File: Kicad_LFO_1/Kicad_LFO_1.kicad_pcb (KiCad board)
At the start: 2 copper layers, 100 x 100 mm, 13 parts, among them J101 LFO555, J102 555 Reset, J103 LFO555Charge, SW101 LFO Low, U101 LM555

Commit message: Sine and tri integrator added
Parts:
- added P101: HEADER_2x5_Doepfer, Connector_IDC:IDC-Header_2x05_P2.54mm_Vertical, F.Cu at (62.0, 144.5)
- added U102: TL072, AJ-Dropbox-Kicad:AJ_SO-8_5.3x6.2mm_P1.27mm, B.Cu at (58.5, 114.5)
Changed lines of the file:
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@@
     (tracks 0)
     (zones 0)
-    (modules 13)
-    (nets 12)
+    (modules 15)
+    (nets 14)
   )
   (page A4)
@@
     (solder_mask_min_width 0.25)
     (aux_axis_origin 0 0)
-    (visible_elements FFFFFF7F)
+    (visible_elements 7FFFFFFF)
     (pcbplotparams
       (layerselection 0x010fc_ffffffff)
@@
   (net 10 "Net-(J102-PadT)")
   (net 11 "Net-(RV101-Pad2)")
+  (net 12 -12V)
+  (net 13 "Net-(P101-Pad10)")
   (net_class Default "This is the default net class."
     (clearance 0.2)
@@
     (uvia_drill 0.1)
     (add_net +12V)
+    (add_net -12V)
     (add_net GND)
     (add_net "Net-(C101-Pad1)")
@@
     (add_net "Net-(J101-PadT)")
     (add_net "Net-(J102-PadT)")
+    (add_net "Net-(P101-Pad10)")
     (add_net "Net-(R101-Pad1)")
     (add_net "Net-(R102-Pad1)")
@@
     (model ${KISYS3DMOD}/Package_SO.3dshapes/SO-8_5.3x6.2mm_P1.27mm.wrl
       (at (xyz 0 0 0))
+      (scale (xyz 1 1 1))
+      (rotate (xyz 0 0 0))
+    )
+    (model C:/Users/anders/Documents/KiCad/Lib/aj_packages3d/kicad-packages3D/Package_SO.3dshapes/SO-8_5.3x6.2mm_P1.27mm.step
+      (at (xyz 0 0 0))
+      (scale (xyz 1 1 1))
+      (rotate (xyz 0 0 0))
+    )
+  )
+  (module Connector_IDC:IDC-Header_2x05_P2.54mm_Vertical (layer F.Cu)
+    (at 62 144.5 180)
+    (descr "Through hole straight IDC box header, 2x05, 2.54mm pitch, double rows")
+    (tags "Through hole IDC box header THT 2x05 2.54mm double row")
+    (fp_text reference P101 (at 1.27 -6.604 180) (layer F.SilkS)
+      (effects (font (size 1 1) (thickness 0.15)))
+    )
+    (fp_text value HEADER_2x5_Doepfer (at 1.27 16.764 180) (layer F.Fab)
+      (effects (font (size 1 1) (thickness 0.15)))
+    )
+    (fp_text user %R (at 1.27 5.08 180) (layer F.Fab)
+      (effects (font (size 1 1) (thickness 0.15)))
+    )
+    (fp_line (start 5.695 -5.1) (end 5.695 15.26) (layer F.Fab) (width 0.1))
+    (fp_line (start 5.145 -4.56) (end 5.145 14.7) (layer F.Fab) (width 0.1))
+    (fp_line (start -3.155 -5.1) (end -3.155 15.26) (layer F.Fab) (width 0.1))
+    (fp_line (start -2.605 -4.56) (end -2.605 2.83) (layer F.Fab) (width 0.1))
+    (fp_line (start -2.605 7.33) (end -2.605 14.7) (layer F.Fab) (width 0.1))
+    (fp_line (start -2.605 2.83) (end -3.155 2.83) (layer F.Fab) (width 0.1))
+    (fp_line (start -2.605 7.33) (end -3.155 7.33) (layer F.Fab) (width 0.1))
+    (fp_line (start 5.695 -5.1) (end -3.155 -5.1) (layer F.Fab) (width 0.1))
+    (fp_line (start 5.145 -4.56) (end -2.605 -4.56) (layer F.Fab) (width 0.1))
+    (fp_line (start 5.695 15.26) (end -3.155 15.26) (layer F.Fab) (width 0.1))
+    (fp_line (start 5.145 14.7) (end -2.605 14.7) (layer F.Fab) (width 0.1))
+    (fp_line (start 5.695 -5.1) (end 5.145 -4.56) (layer F.Fab) (width 0.1))
+    (fp_line (start 5.695 15.26) (end 5.145 14.7) (layer F.Fab) (width 0.1))
+    (fp_line (start -3.155 -5.1) (end -2.605 -4.56) (layer F.Fab) (width 0.1))
+    (fp_line (start -3.155 15.26) (end -2.605 14.7) (layer F.Fab) (width 0.1))
+    (fp_line (start 5.95 -5.35) (end 5.95 15.51) (layer F.CrtYd) (width 0.05))
+    (fp_line (start 5.95 15.51) (end -3.41 15.51) (layer F.CrtYd) (width 0.05))
+    (fp_line (start -3.41 15.51) (end -3.41 -5.35) (layer F.CrtYd) (width 0.05))
+    (fp_line (start -3.41 -5.35) (end 5.95 -5.35) (layer F.CrtYd) (width 0.05))
+    (fp_line (start 5.945 -5.35) (end 5.945 15.51) (layer F.SilkS) (width 0.12))
+    (fp_line (start 5.945 15.51) (end -3.405 15.51) (layer F.SilkS) (width 0.12))
+    (fp_line (start -3.405 15.51) (end -3.405 -5.35) (layer F.SilkS) (width 0.12))
+    (fp_line (start -3.405 -5.35) (end 5.945 -5.35) (layer F.SilkS) (width 0.12))
+    (fp_line (start -3.655 -5.6) (end -3.655 -3.06) (layer F.SilkS) (width 0.12))
+    (fp_line (start -3.655 -5.6) (end -1.115 -5.6) (layer F.SilkS) (width 0.12))
+    (pad 1 thru_hole rect (at 0 0 180) (size 1.7272 1.7272) (drill 1.016) (layers *.Cu *.Mask)
+      (net 12 -12V))
+    (pad 2 thru_hole oval (at 2.54 0 180) (size 1.7272 1.7272) (drill 1.016) (layers *.Cu *.Mask)
+      (net 12 -12V))
+    (pad 3 thru_hole oval (at 0 2.54 180) (size 1.7272 1.7272) (drill 1.016) (layers *.Cu *.Mask)
+      (net 1 GND))
+    (pad 4 thru_hole oval (at 2.54 2.54 180) (size 1.7272 1.7272) (drill 1.016) (layers *.Cu *.Mask)
+      (net 1 GND))
+    (pad 5 thru_hole oval (at 0 5.08 180) (size 1.7272 1.7272) (drill 1.016) (layers *.Cu *.Mask)
+      (net 1 GND))
+    (pad 6 thru_hole oval (at 2.54 5.08 180) (size 1.7272 1.7272) (drill 1.016) (layers *.Cu *.Mask)
+      (net 1 GND))
+    (pad 7 thru_hole oval (at 0 7.62 180) (size 1.7272 1.7272) (drill 1.016) (layers *.Cu *.Mask)
+      (net 1 GND))
+    (pad 8 thru_hole oval (at 2.54 7.62 180) (size 1.7272 1.7272) (drill 1.016) (layers *.Cu *.Mask)
+      (net 1 GND))
+    (pad 9 thru_hole oval (at 0 10.16 180) (size 1.7272 1.7272) (drill 1.016) (layers *.Cu *.Mask)
+      (net 13 "Net-(P101-Pad10)"))
+    (pad 10 thru_hole oval (at 2.54 10.16 180) (size 1.7272 1.7272) (drill 1.016) (layers *.Cu *.Mask)
+      (net 13 "Net-(P101-Pad10)"))
+    (model ${KISYS3DMOD}/Connector_IDC.3dshapes/IDC-Header_2x05_P2.54mm_Vertical.wrl
+      (at (xyz 0 0 0))
+      (scale (xyz 1 1 1))
+      (rotate (xyz 0 0 0))
+    )
+  )
+  (module AJ-Dropbox-Kicad:AJ_SO-8_5.3x6.2mm_P1.27mm (layer B.Cu)
+    (at 58.5 114.5)
+    (descr "8-Lead Plastic Small Outline, 5.3x6.2mm Body (http://www.ti.com.cn/cn/lit/ds/symlink/tl7705a.pdf)")
+    (tags "SOIC 1.27")
+    (attr smd)
+    (fp_text reference U102 (at 0 4.13) (layer B.SilkS)
+      (effects (font (size 1 1) (thickness 0.15)) (justify mirror))
+    )
+    (fp_text value TL072 (at 0 -4.13) (layer B.Fab)
+      (effects (font (size 1 1) (thickness 0.15)) (justify mirror))
+    )
+    (fp_text user %R (at 0 0) (layer B.Fab)
+      (effects (font (size 1 1) (thickness 0.15)) (justify mirror))
+    )
+    (fp_line (start -1.65 3.1) (end 2.65 3.1) (layer B.Fab) (width 0.15))
+    (fp_line (start 2.65 3.1) (end 2.65 -3.1) (layer B.Fab) (width 0.15))
+    (fp_line (start 2.65 -3.1) (end -2.65 -3.1) (layer B.Fab) (width 0.15))
+    (fp_line (start -2.65 -3.1) (end -2.65 2.1) (layer B.Fab) (width 0.15))
+    (fp_line (start -2.65 2.1) (end -1.65 3.1) (layer B.SilkS) (width 0.15))
+    (fp_line (start -4.83 3.35) (end -4.83 -3.35) (layer B.CrtYd) (width 0.05))
+    (fp_line (start 4.83 3.35) (end 4.83 -3.35) (layer B.CrtYd) (width 0.05))
+    (fp_line (start -4.83 3.35) (end 4.83 3.35) (layer B.CrtYd) (width 0.05))
+    (fp_line (start -4.83 -3.35) (end 4.83 -3.35) (layer B.CrtYd) (width 0.05))
+    (fp_line (start -2.75 3.205) (end -2.75 2.55) (layer B.SilkS) (width 0.15))
+    (fp_line (start 2.75 3.205) (end 2.75 2.455) (layer B.SilkS) (width 0.15))
+    (fp_line (start 2.75 -3.205) (end 2.75 -2.455) (layer B.SilkS) (width 0.15))
+    (fp_line (start -2.75 -3.205) (end -2.75 -2.455) (layer B.SilkS) (width 0.15))
+    (fp_line (start -2.75 3.205) (end 2.75 3.205) (layer B.SilkS) (width 0.15))
+    (fp_line (start -2.75 -3.205) (end 2.75 -3.205) (layer B.SilkS) (width 0.15))
+    (fp_line (start -2.75 2.55) (end -4.5 2.55) (layer B.SilkS) (width 0.15))
+    (fp_line (start 2.794 2.54) (end 4.572 2.54) (layer B.SilkS) (width 0.15))
+    (fp_line (start 4.572 2.54) (end 4.572 -2.54) (layer B.SilkS) (width 0.15))
+    (fp_line (start 4.572 -2.54) (end 2.794 -2.54) (layer B.SilkS) (width 0.15))
+    (fp_line (start -2.794 -2.54) (end -4.572 -2.54) (layer B.SilkS) (width 0.15))
+    (fp_line (start -4.572 -2.54) (end -4.572 2.54) (layer B.SilkS) (width 0.15))
+    (fp_text user * (at -3.81 3.048) (layer B.SilkS)
+      (effects (font (size 1 1) (thickness 0.15)) (justify mirror))
+    )
+    (pad 1 smd rect (at -3.3 1.905) (size 2 0.55) (layers B.Cu B.Paste B.Mask))
+    (pad 2 smd rect (at -3.3 0.635) (size 2 0.55) (layers B.Cu B.Paste B.Mask))
+    (pad 3 smd rect (at -3.3 -0.635) (size 2 0.55) (layers B.Cu B.Paste B.Mask))
+    (pad 4 smd rect (at -3.3 -1.905) (size 2 0.55) (layers B.Cu B.Paste B.Mask)
+      (net 12 -12V))
+    (pad 5 smd rect (at 3.3 -1.905) (size 2 0.55) (layers B.Cu B.Paste B.Mask))
+    (pad 6 smd rect (at 3.3 -0.635) (size 2 0.55) (layers B.Cu B.Paste B.Mask))
+    (pad 7 smd rect (at 3.3 0.635) (size 2 0.55) (layers B.Cu B.Paste B.Mask))
+    (pad 8 smd rect (at 3.3 1.905) (size 2 0.55) (layers B.Cu B.Paste B.Mask)
+      (net 13 "Net-(P101-Pad10)"))
+    (model ${KISYS3DMOD}/Package_SO.3dshapes/SO-8_5.3x6.2mm_P1.27mm.wrl
+      (at (xyz 0 0 0))

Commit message: Update Kicad_LFO_1.kicad_pcb
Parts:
- added C104: 4u7, Capacitor_SMD:C_1206_3216Metric_Pad1.42x1.75mm_HandSolder, B.Cu at (44.5, 108.1)
- added C105: 4u7, Capacitor_SMD:C_1206_3216Metric_Pad1.42x1.75mm_HandSolder, B.Cu at (38.6, 108.1)
- added C106: 470n, Capacitor_SMD:C_0805_2012Metric_Pad1.15x1.40mm_HandSolder, B.Cu at (27.2, 122.0)
- added D101: 1N4148W, Diode_SMD:D_SOD-123, B.Cu at (32.7, 108.1)
- added D102: 1N4148W, Diode_SMD:D_SOD-123, B.Cu at (27.0, 108.1)
- added J104: Tri, AJ-Dropbox-Kicad:AudioJack3StereoNarrow-PJ-321, F.Cu at (55.5, 119.0)
- added J105: Sine, AJ-Dropbox-Kicad:AudioJack3StereoNarrow-PJ-321, F.Cu at (55.5, 146.0)
- added R105: 100k, Resistor_SMD:R_0805_2012Metric_Pad1.15x1.40mm_HandSolder, B.Cu at (18.1, 107.4)
- added R106: 10k, Resistor_SMD:R_0805_2012Metric_Pad1.15x1.40mm_HandSolder, B.Cu at (27.2, 124.9)
- added R107: 1k, Resistor_SMD:R_0805_2012Metric_Pad1.15x1.40mm_HandSolder, B.Cu at (27.2, 127.9)
- added R108: 10k, Resistor_SMD:R_0805_2012Metric_Pad1.15x1.40mm_HandSolder, B.Cu at (21.7, 110.3)
- added R109: 1k, Resistor_SMD:R_0805_2012Metric_Pad1.15x1.40mm_HandSolder, B.Cu at (27.2, 130.8)
- added R110: 10k, Resistor_SMD:R_0805_2012Metric_Pad1.15x1.40mm_HandSolder, B.Cu at (13.3, 107.4)
- added R111: 10k, Resistor_SMD:R_0805_2012Metric_Pad1.15x1.40mm_HandSolder, B.Cu at (17.0, 110.3)
- added RV102: 10k Sine, Potentiometer_THT:Potentiometer_Alps_RK163_Single_Horizontal, F.Cu at (54.0, 127.5)
- P101: moved to B.Cu
- moved P101 31.1 mm to (59.5, 113.5), turned to 0 degrees
- moved U102 8.00 mm to (58.5, 122.5)
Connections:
- net Net-(C102-Pad1) renamed Charge
- net Net-(J101-PadT) renamed Square
- net Net-(J102-PadT) renamed Reset
- U102 pad 1: (no net) -> Tri
- U102 pad 2: (no net) -> Net-(C106-Pad2)
- U102 pad 3: (no net) -> GND
- U102 pad 5: (no net) -> Net-(R109-Pad2)
- U102 pad 6: (no net) -> Net-(R107-Pad2)
- U102 pad 7: (no net) -> Sine

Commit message: Update Kicad_LFO_1.kicad_pcb
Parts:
- C103, P101: moved to F.Cu
- moved D102 41.0 mm to (62.5, 128.5), turned to 90 degrees
- moved R105 36.8 mm to (54.0, 115.5), turned to 270 degrees
- moved D101 33.6 mm to (59.5, 128.5), turned to 270 degrees
- moved R110 32.4 mm to (39.5, 126.5)
- moved C106 30.0 mm to (56.5, 115.5), turned to 90 degrees
- moved R106 30.0 mm to (54.0, 111.5), turned to 270 degrees
- moved R109 29.9 mm to (57.0, 128.5), turned to 270 degrees
- moved R108 25.5 mm to (44.2, 122.3)
- moved R111 25.5 mm to (39.5, 122.3)
- moved C105 23.5 mm to (62.0, 109.5), turned to 270 degrees
- moved C104 19.4 mm to (62.0, 116.5), turned to 270 degrees
- moved U102 14.0 mm to (59.5, 136.5), turned to 90 degrees
- moved R103 10.6 mm to (64.0, 80.0)
- moved P101 7.43 mm to (64.5, 108.0)
- moved U101 7.11 mm to (64.5, 72.5), turned to 90 degrees
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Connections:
- C104 pad 2: Net-(C104-Pad2) -> +12V
- P101 pad 10: Net-(C104-Pad2) -> +12V
- P101 pad 9: Net-(C104-Pad2) -> +12V
- U102 pad 8: Net-(C104-Pad2) -> +12V
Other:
- outline, holes or cut-outs redrawn

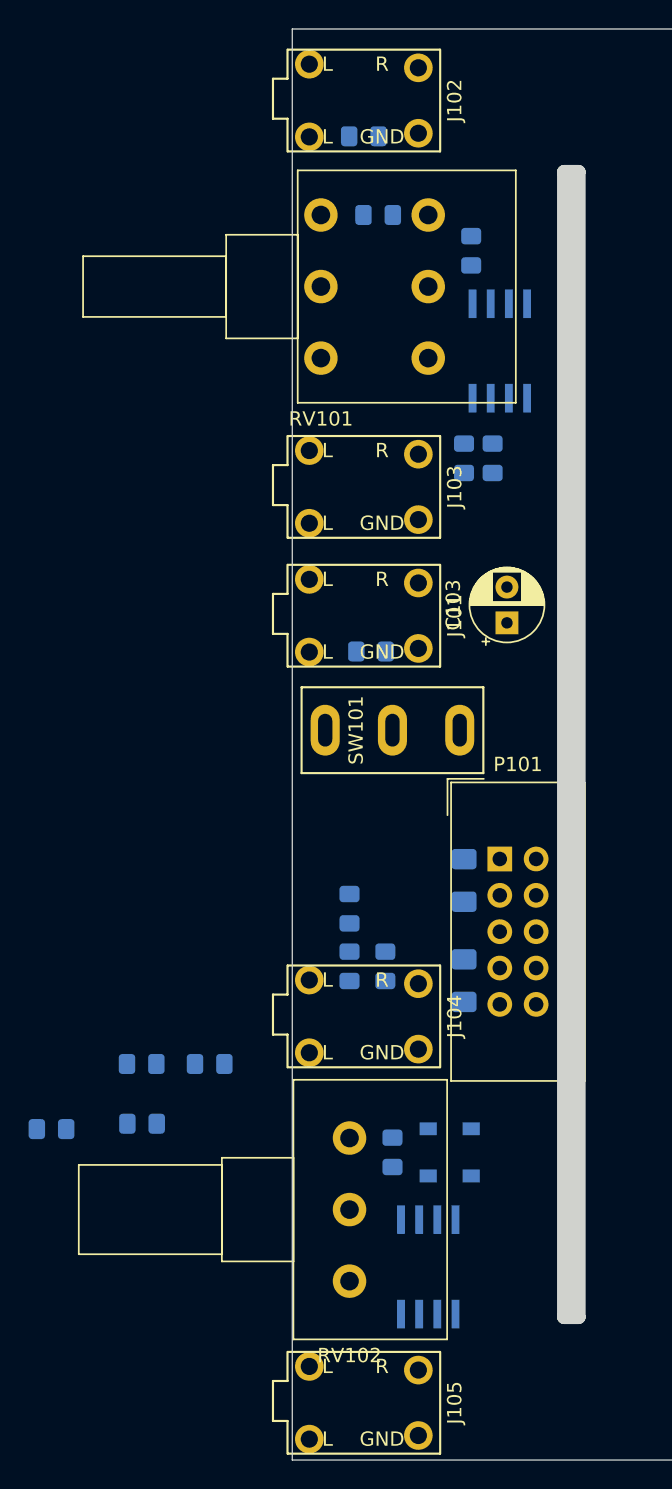
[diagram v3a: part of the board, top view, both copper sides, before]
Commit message: Routed 555 LFO
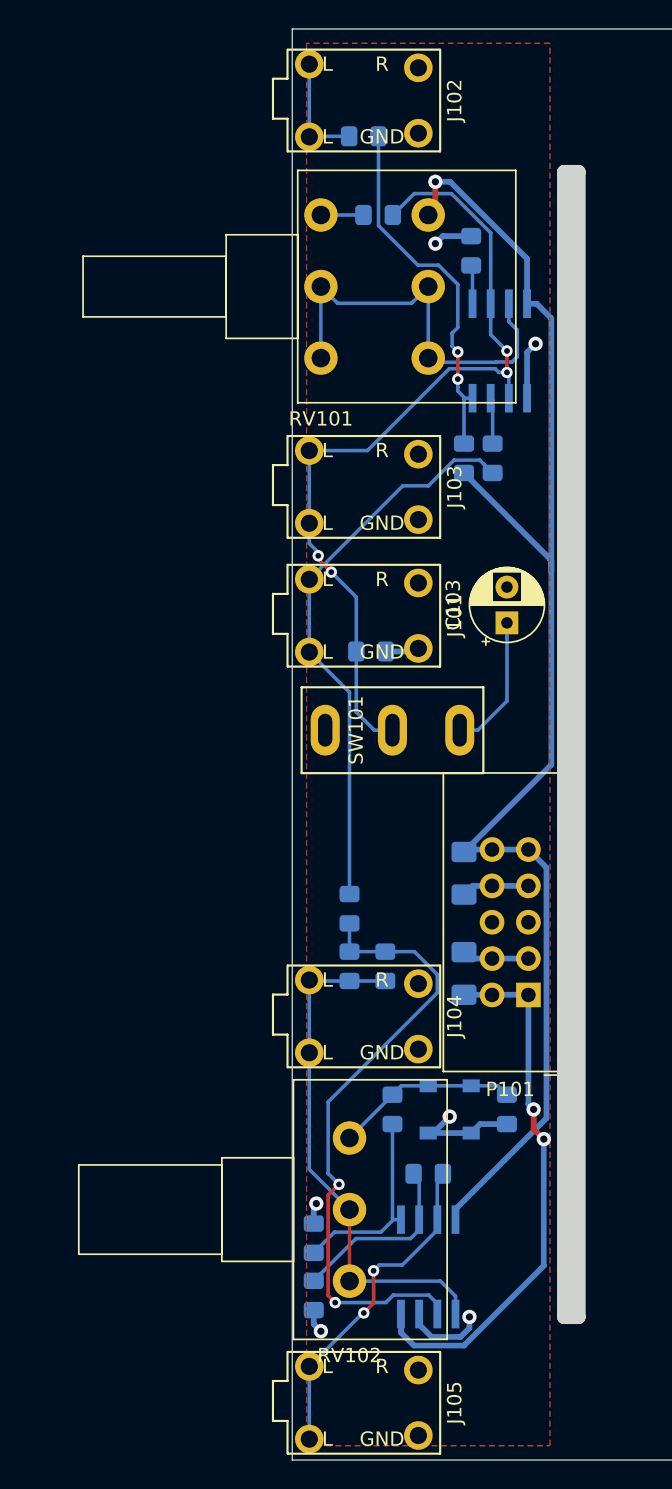
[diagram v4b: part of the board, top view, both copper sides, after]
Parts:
- moved R110 25.5 mm to (65.0, 125.5), turned to 90 degrees
- moved R107 21.7 mm to (51.5, 138.5), turned to 90 degrees
- moved R111 17.1 mm to (51.5, 134.5), turned to 270 degrees
- moved R108 17.1 mm to (59.5, 130.0), turned to 0 degrees
- moved P101 9.71 mm to (66.5, 117.5), turned to 180 degrees
- moved C104 7.50 mm to (62.0, 109.0), turned to 90 degrees
- moved C105 6.50 mm to (62.0, 116.0), turned to 90 degrees
- moved D101 3.00 mm to (59.5, 125.5)
- moved D102 3.00 mm to (62.5, 125.5)
- moved R109 3.00 mm to (57.0, 125.5)
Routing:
- net +12V: track 0.00 -> 99.7 mm, vias 0 -> 1
- net Charge: track 0.00 -> 59.6 mm, vias 0 -> 4
- net Net-(C106-Pad2): track 0.00 -> 44.0 mm, vias 0 -> 2
- net Square: track 0.00 -> 39.8 mm
- net -12V: track 0.00 -> 38.3 mm, vias 0 -> 2
- net Tri: track 0.00 -> 36.6 mm
- net GND: track 0.00 -> 36.1 mm, vias 0 -> 6
- net Net-(RV101-Pad2): track 0.00 -> 28.9 mm
- net Net-(R102-Pad1): track 0.00 -> 25.7 mm, vias 0 -> 2
- net Sine: track 0.00 -> 23.4 mm, vias 0 -> 2
- net Net-(R109-Pad2): track 0.00 -> 13.8 mm
- net Net-(R107-Pad2): track 0.00 -> 12.9 mm
- net Net-(D101-Pad1): track 0.00 -> 12.8 mm
- net Net-(C103-Pad1): track 0.00 -> 9.61 mm
- net Reset: track 0.00 -> 7.88 mm
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- added copper zone on F.Cu, net GND
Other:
- net class Power added: clearance 0.2, trace_width 0.4, via_dia 1, via_drill 0.5

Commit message: Update Kicad_LFO_1.kicad_pcb
3D
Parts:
- added G***: LOGO, AJ:Johansen_engineering_logo_15mm, B.Cu at (66.0, 57.0)
- added G***: LOGO, AJ:Johansen_engineering_logo_15mm, F.Cu at (66.0, 57.0)
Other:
- board text added: "JE 555 LFO 1 2019/03/19 Rev A"
- board text added: "Johansen Engineering 2019/03/19 - Rev A 555 LFO 1"

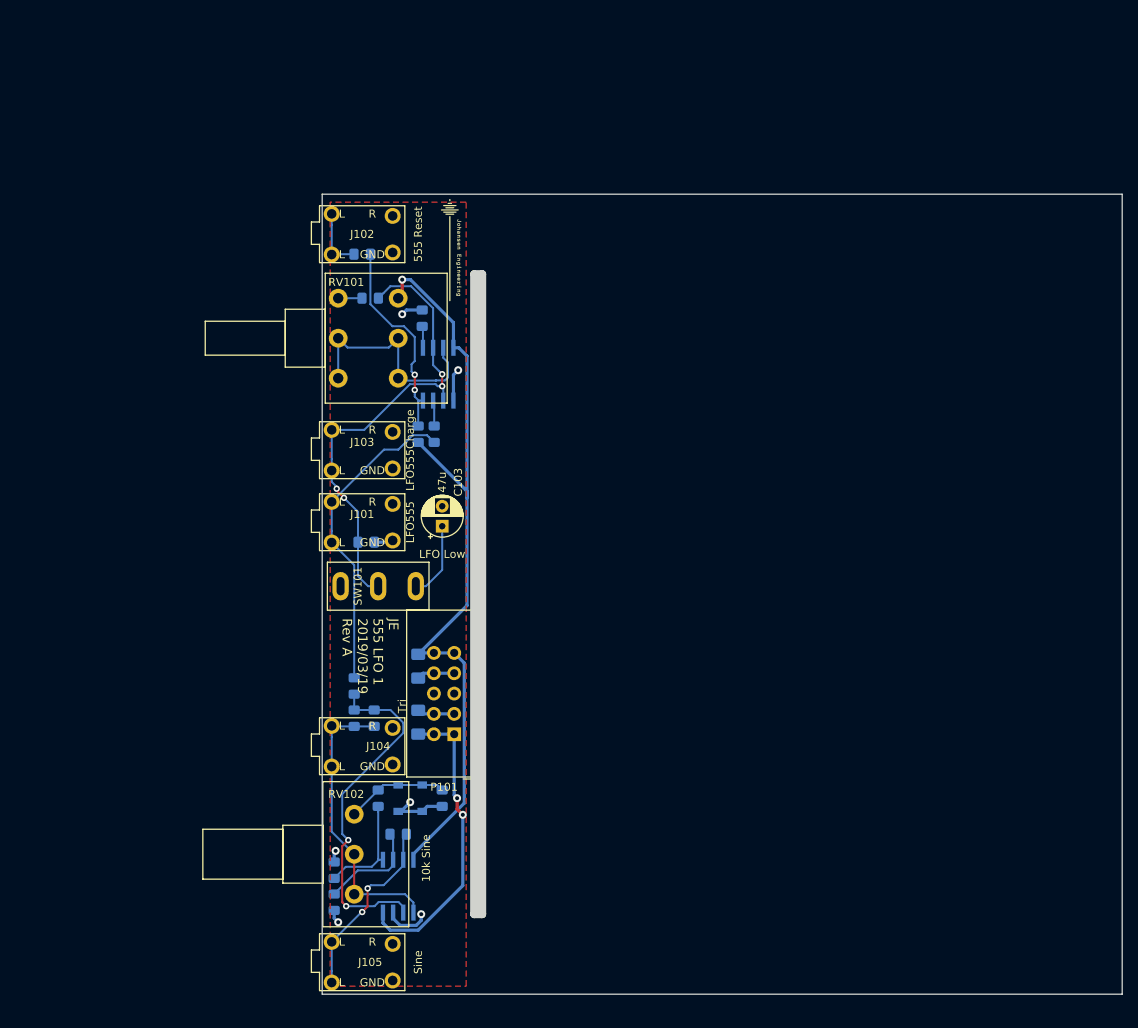
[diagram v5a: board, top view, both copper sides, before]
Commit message: PCB bottom layer Vcc
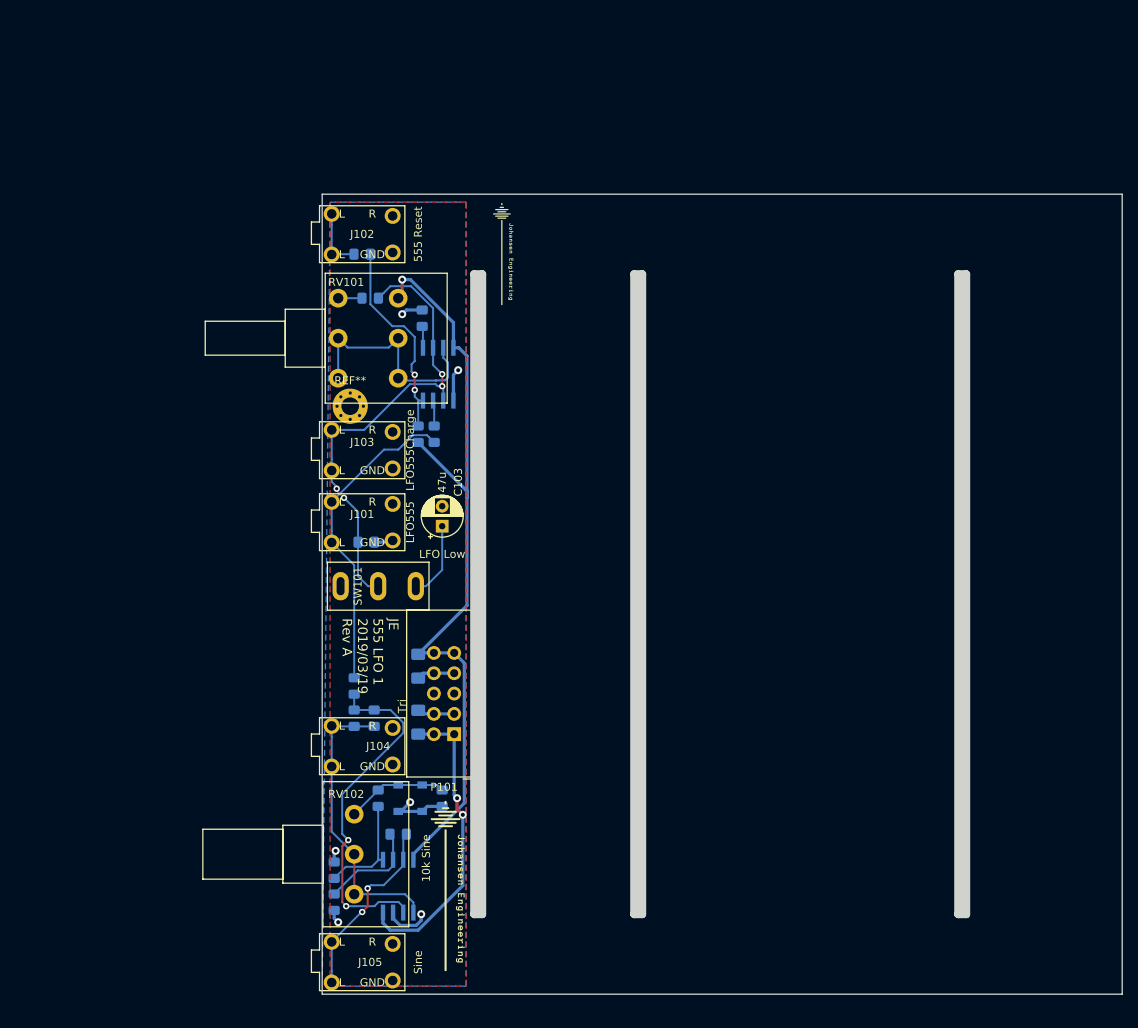
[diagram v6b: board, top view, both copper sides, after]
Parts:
- added G***: LOGO, AJ:Johansen_engineering_logo_25mm_front_neg5, F.Cu at (65.5, 136.5)
- added REF**: MountingHole_2.2mm_M2_Pad_Via, MountingHole:MountingHole_2.2mm_M2_Pad_Via, F.Cu at (53.5, 76.5)
- moved G*** 6.52 mm to (72.5, 57.5)
- moved G*** 1.00 mm to (66.0, 58.0)
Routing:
- added copper zone on B.Cu, net +12V
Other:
- outline, holes or cut-outs redrawn
